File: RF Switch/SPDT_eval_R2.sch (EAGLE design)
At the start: 10 parts, among them J4 22-23-2051, U1 QPC1022

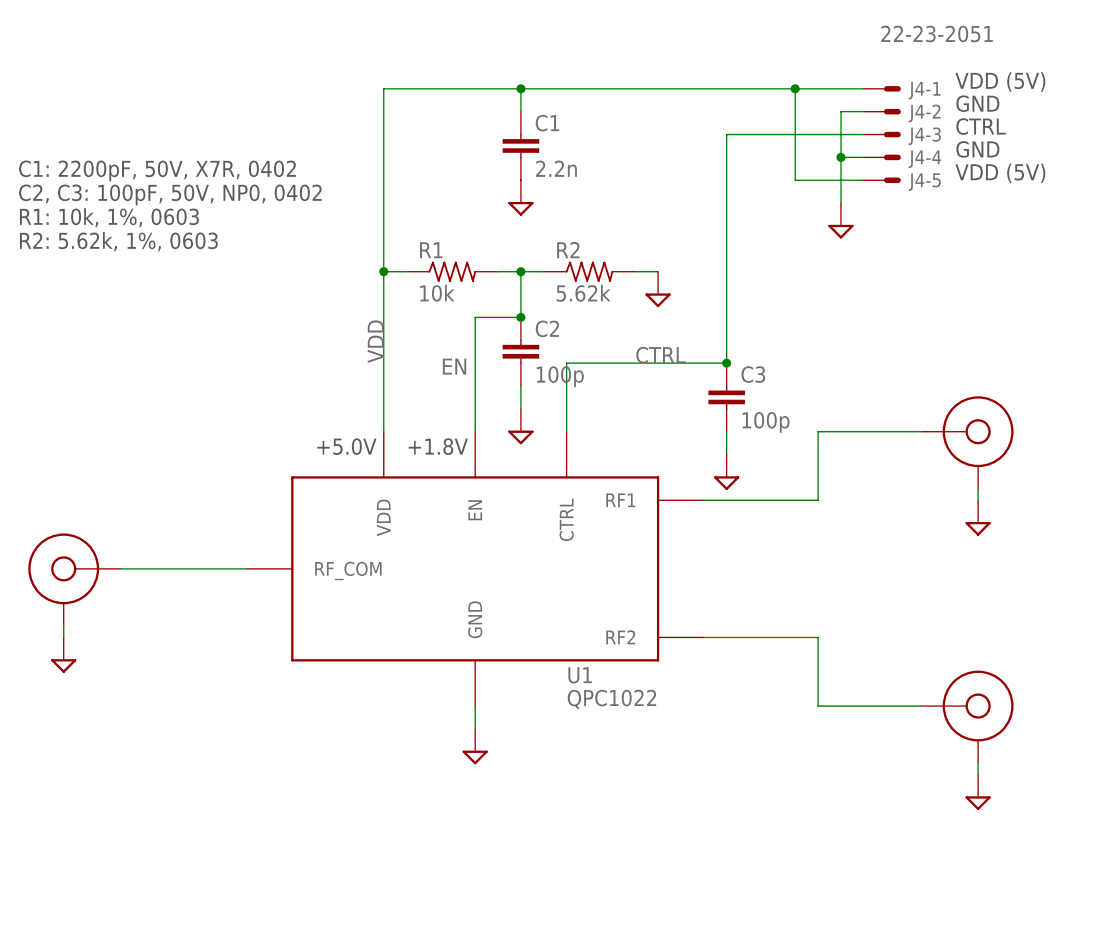
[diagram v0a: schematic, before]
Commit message: Added mounting holes, cleaned up text a bit.
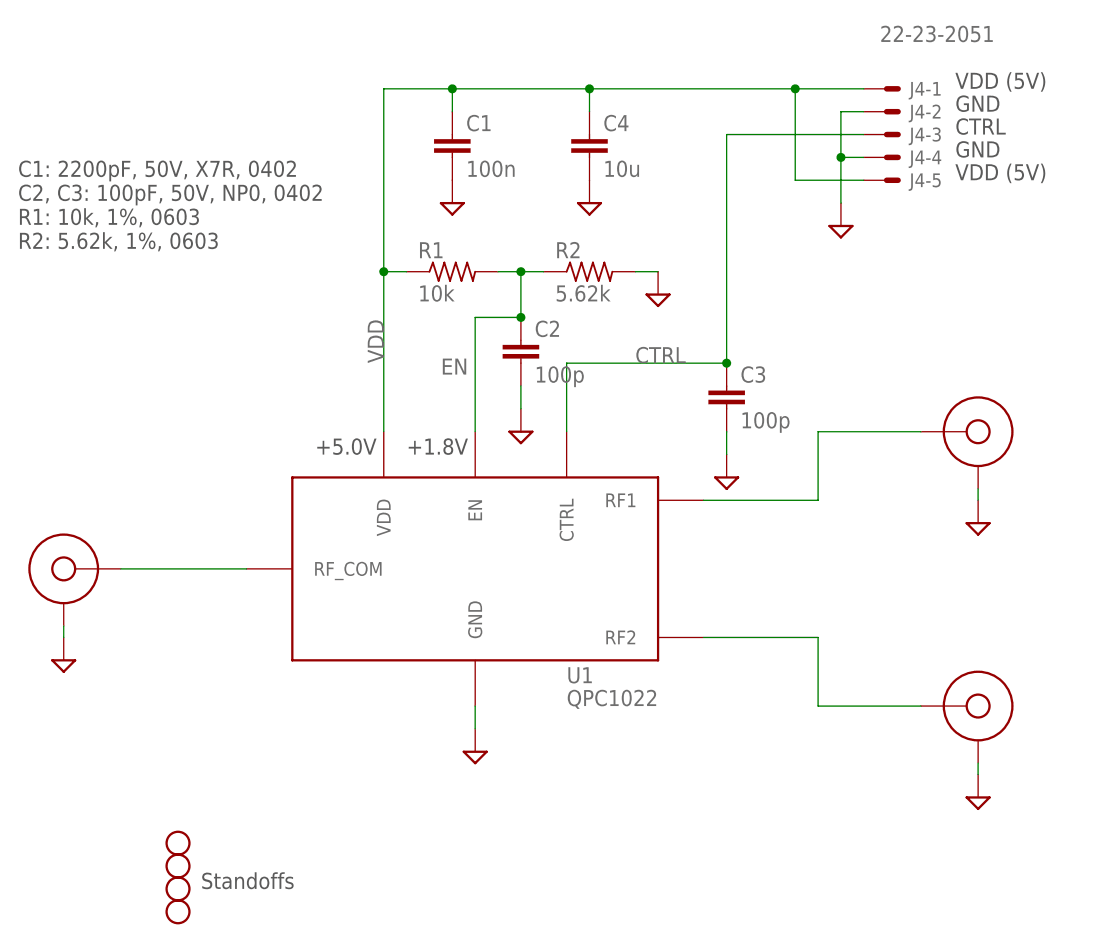
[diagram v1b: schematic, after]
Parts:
- added C4: 10u, rcl_custom:C-EU0805-B-NOSILK
- added H1, H2, H3, H4: STAND-OFFTIGHT, SparkFun-Hardware:STAND-OFFTIGHT
- C1: value 2.2n -> 100n
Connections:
- net GND: now also C4.2
- net VDD: now also C4.1
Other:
- note added: "Standoffs"
- moved on the sheet: C1
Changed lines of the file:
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@@
 <?xml version="1.0" encoding="utf-8"?>
 <!DOCTYPE eagle SYSTEM "eagle.dtd">
-<eagle version="8.5.0">
+<eagle version="8.5.1">
 <drawing>
 <settings>
@@
 <setting verticaltext="up"/>
 </settings>
-<grid distance="0.05" unitdist="inch" unit="inch" style="lines" multiple="2" display="yes" altdistance="0.01" altunitdist="inch" altunit="inch"/>
+<grid distance="0.1" unitdist="inch" unit="inch" style="lines" multiple="1" display="no" altdistance="0.01" altunitdist="inch" altunit="inch"/>
 <layers>
 <layer number="1" name="Top" color="4" fill="1" visible="no" active="no"/>
@@
 <layer number="58" name="b3D" color="7" fill="1" visible="no" active="no"/>
 <layer number="59" name="Invisible" color="7" fill="1" visible="no" active="no"/>
+<layer number="60" name="bCarbon" color="7" fill="1" visible="no" active="no"/>
 <layer number="61" name="stand" color="7" fill="1" visible="no" active="no"/>
 <layer number="88" name="SimResults" color="9" fill="1" visible="yes" active="yes"/>
@@
 <layer number="127" name="_tValues" color="7" fill="1" visible="yes" active="yes"/>
 <layer number="128" name="_bValues" color="7" fill="1" visible="yes" active="yes"/>
+<layer number="129" name="Mask" color="7" fill="1" visible="yes" active="yes"/>
 <layer number="130" name="bLogo" color="7" fill="1" visible="yes" active="yes"/>
 <layer number="131" name="tAdjust" color="7" fill="1" visible="yes" active="yes"/>
@@
 <layer number="227" name="227bmp" color="7" fill="1" visible="yes" active="yes"/>
 <layer number="228" name="228bmp" color="7" fill="1" visible="yes" active="yes"/>
+<layer number="229" name="229bmp" color="7" fill="1" visible="yes" active="yes"/>
+<layer number="230" name="230bmp" color="7" fill="1" visible="yes" active="yes"/>
 <layer number="231" name="Eagle3D_PG1" color="7" fill="1" visible="yes" active="yes"/>
 <layer number="232" name="Eagle3D_PG2" color="7" fill="1" visible="yes" active="yes"/>
@@
 <layer number="251" name="SMDround" color="7" fill="1" visible="yes" active="yes"/>
 <layer number="254" name="cooling" color="7" fill="1" visible="yes" active="yes"/>
+<layer number="255" name="routoute" color="7" fill="1" visible="yes" active="yes"/>
 </layers>
 <schematic xreflabel="%F%N/%S.%C%R" xrefpart="/%S.%C%R">
@@
 <part name="J4" library="con-molex" library_urn="urn:adsk.eagle:library:165" deviceset="22-23-2051" device=""/>
 <part name="U1" library="QPC1022" deviceset="QPC1022" device=""/>
-<part name="C1" library="rcl_custom" deviceset="C-EU" device="0402-B-NOSILK" value="2.2n"/>
+<part name="C1" library="rcl_custom" deviceset="C-EU" device="0402-B-NOSILK" value="100n"/>
 <part name="C2" library="rcl_custom" deviceset="C-EU" device="0402-B-NOSILK" value="100p"/>
 <part name="C3" library="rcl_custom" deviceset="C-EU" device="0402-B-NOSILK" value="100p"/>
@@
 <part name="CF2" library="psas_c3_team05" deviceset="SMA-CINCH-END-FIRE" device=""/>
 <part name="CF3" library="psas_c3_team05" deviceset="SMA-CINCH-END-FIRE" device=""/>
+<part name="H1" library="SparkFun-Hardware" library_urn="urn:adsk.eagle:library:519" deviceset="STAND-OFF" device="TIGHT" package3d_urn="urn:adsk.eagle:package:38629/1"/>
+<part name="H2" library="SparkFun-Hardware" library_urn="urn:adsk.eagle:library:519" deviceset="STAND-OFF" device="TIGHT" package3d_urn="urn:adsk.eagle:package:38629/1"/>
+<part name="H3" library="SparkFun-Hardware" library_urn="urn:adsk.eagle:library:519" deviceset="STAND-OFF" device="TIGHT" package3d_urn="urn:adsk.eagle:package:38629/1"/>
+<part name="H4" library="SparkFun-Hardware" library_urn="urn:adsk.eagle:library:519" deviceset="STAND-OFF" device="TIGHT" package3d_urn="urn:adsk.eagle:package:38629/1"/>
+<part name="C4" library="rcl_custom" deviceset="C-EU" device="0805-B-NOSILK" value="10u"/>
+<part name="SUPPLY10" library="supply2" library_urn="urn:adsk.eagle:library:372" deviceset="GND" device=""/>
 </parts>
 <sheets>
@@
 <text x="177.8" y="137.16" size="1.778" layer="97">VDD (5V)</text>
 <text x="177.8" y="142.24" size="1.778" layer="97">CTRL</text>
+<text x="93.98" y="58.42" size="1.778" layer="97">Standoffs</text>
 </plain>
 <instances>
@@
 <attribute name="VALUE" x="134.62" y="78.74" size="1.778" layer="96"/>
 </instance>
-<instance part="C1" gate="CE" x="129.54" y="142.24"/>
+<instance part="C1" gate="CE" x="121.92" y="142.24"/>
 <instance part="C2" gate="CE" x="129.54" y="119.38"/>
 <instance part="C3" gate="CE" x="152.4" y="114.3"/>
@@
 <instance part="R2" gate="R" x="137.16" y="127"/>
 <instance part="SUPPLY6" gate="GND" x="144.78" y="124.46" smashed="yes"/>
-<instance part="SUPPLY7" gate="GND" x="129.54" y="134.62" smashed="yes"/>
+<instance part="SUPPLY7" gate="GND" x="121.92" y="134.62" smashed="yes"/>
 <instance part="SUPPLY8" gate="GND" x="129.54" y="109.22" smashed="yes"/>
 <instance part="SUPPLY9" gate="GND" x="152.4" y="104.14" smashed="yes"/>
@@
 <attribute name="NAME" x="176.53" y="74.93" size="1.778" layer="104" rot="MR0"/>
 </instance>
+<instance part="H1" gate="G$1" x="91.44" y="63.5"/>
+<instance part="H2" gate="G$1" x="91.44" y="60.96"/>
+<instance part="H3" gate="G$1" x="91.44" y="58.42"/>
+<instance part="H4" gate="G$1" x="91.44" y="55.88"/>
+<instance part="C4" gate="CE" x="137.16" y="142.24"/>
+<instance part="SUPPLY10" gate="GND" x="137.16" y="134.62" smashed="yes"/>
 </instances>
 <busses>
@@
 <wire x1="180.34" y1="71.12" x2="180.34" y2="72.39" width="0.1524" layer="91"/>
 </segment>
+<segment>
+<pinref part="C4" gate="CE" pin="2"/>
+<pinref part="SUPPLY10" gate="GND" pin="GND"/>
+</segment>
 </net>
 <net name="RF2" class="1">
@@
 <pinref part="J4" gate="-1" pin="S"/>
 <wire x1="167.64" y1="147.32" x2="160.02" y2="147.32" width="0.1524" layer="91"/>
-<wire x1="160.02" y1="147.32" x2="129.54" y2="147.32" width="0.1524" layer="91"/>
+<wire x1="160.02" y1="147.32" x2="137.16" y2="147.32" width="0.1524" layer="91"/>
 <pinref part="J4" gate="-5" pin="S"/>
-<wire x1="129.54" y1="147.32" x2="114.3" y2="147.32" width="0.1524" layer="91"/>
+<wire x1="137.16" y1="147.32" x2="121.92" y2="147.32" width="0.1524" layer="91"/>
+<wire x1="121.92" y1="147.32" x2="114.3" y2="147.32" width="0.1524" layer="91"/>
 <wire x1="167.64" y1="137.16" x2="160.02" y2="137.16" width="0.1524" layer="91"/>
 <wire x1="160.02" y1="137.16" x2="160.02" y2="147.32" width="0.1524" layer="91"/>
@@
 <junction x="114.3" y="127"/>
 <pinref part="C1" gate="CE" pin="1"/>
-<wire x1="129.54" y1="144.78" x2="129.54" y2="147.32" width="0.1524" layer="91"/>
-<junction x="129.54" y="147.32"/>
+<wire x1="121.92" y1="144.78" x2="121.92" y2="147.32" width="0.1524" layer="91"/>
+<junction x="121.92" y="147.32"/>
 <label x="114.3" y="116.84" size="1.778" layer="95" rot="R90"/>
+<pinref part="C4" gate="CE" pin="1"/>
+<wire x1="137.16" y1="144.78" x2="137.16" y2="147.32" width="0.1524" layer="91"/>
+<junction x="137.16" y="147.32"/>
 </segment>
 </net>
@@
 will not be understood (or retained) with this version.
 </note>
+<note version="8.3" severity="warning">
+Since Version 8.3, EAGLE supports the association of 3D packages
+with devices in libraries, schematics, and board files. Those 3D
+packages will not be understood (or retained) with this version.
+</note>
 </compatibility>
